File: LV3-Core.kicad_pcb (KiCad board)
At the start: 2 copper layers, 114.3 x 59.1 mm, 81 parts, among them IC1 TLV74033PDBVR, J1 Conn_01x02_Pin, J2 USB_C_Receptacle_USB2.0_16P, J3 Conn_01x01, J4 Conn_01x40_Socket, J5 Conn_01x05_Pin, J6 Conn_01x05_Pin, J7 Conn_01x01, J8 FTSH-105-01-L-DV-K-A, J9 Conn_01x02_Pin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

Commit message: layout almost complete
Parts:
- D1: footprint Package_TO_SOT_SMD:SOT-23_Handsoldering -> Package_TO_SOT_SMD:SOT-23W
- D2, D5: footprint Diode_SMD:D_SOD-323 -> Diode_SMD:D_SOD-323_HandSoldering
- moved C19 71.7 mm to (164.8, 96.8), turned to -135 degrees
- moved D6 36.7 mm to (125.1, 80.0), turned to 180 degrees
- moved R2 33.6 mm to (163.6, 69.6), turned to 90 degrees
- moved R9 33.4 mm to (99.8, 85.6), turned to 90 degrees
- moved R5 33.3 mm to (176.3, 69.6), turned to 90 degrees
- moved C28 32.1 mm to (150.9, 77.2), turned to 0 degrees
- moved C11 31.8 mm to (165.4, 69.6), turned to -90 degrees
- moved C12 31.7 mm to (177.9, 69.6), turned to -90 degrees
- moved R18 30.1 mm to (146.8, 97.3), turned to 0 degrees
- moved D2 29.3 mm to (99.8, 91.7), turned to -90 degrees
- moved D3 29.2 mm to (125.1, 75.6)
- moved IC1 29.0 mm to (149.1, 80.3), turned to -90 degrees
- moved U4 29.0 mm to (100.8, 75.4)
- moved S3 29.0 mm to (182.9, 68.6), turned to 0 degrees
- moved R8 28.9 mm to (98.9, 88.4)
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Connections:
- R6 pad 1: PRIMARY_CAN- -> PRIMARY_CAN+
- R7 pad 1: AUX_CAN- -> AUX_CAN+
- S4 pad 2: PRIMARY_CAN+ -> PRIMARY_CAN-
- S5 pad 2: AUX_CAN+ -> AUX_CAN-
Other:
- board size 114.3 x 59.1 mm -> 114.3 x 57.2 mm
- board text added: "+"
- board text added: "-"
- board text added: "12V"
- board text added: "5V"
- board text added: "AUX CAN"
- board text added: "AUX CAN TERMINATION"
- board text added: "BOOT0 PB8"
- board text added: "CAN+"
- board text added: "CAN-"
- board text added: "GND"
- board text added: "OFF"
- board text added: "ON"
- board text added: "PRIMARY CAN TERMINATION"
- board text added: "RESET"
- board text added: "SWD"
- board text added: "USR1 PC13"

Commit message: completed layout and routing
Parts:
- added D10: LED, LED_SMD:LED_0603_1608Metric_Pad1.05x0.95mm_HandSolder, F.Cu at (106.7, 66.0)
- added D11: LED, LED_SMD:LED_0603_1608Metric_Pad1.05x0.95mm_HandSolder, F.Cu at (116.8, 66.0)
- added D12: LED, LED_SMD:LED_0603_1608Metric_Pad1.05x0.95mm_HandSolder, F.Cu at (127.0, 66.0)
- added D9: LED, LED_SMD:LED_0603_1608Metric_Pad1.05x0.95mm_HandSolder, F.Cu at (169.9, 79.0)
- added R21: 470, Resistor_SMD:R_0603_1608Metric_Pad0.98x0.95mm_HandSolder, F.Cu at (169.9, 80.8)
- added R22: 470, Resistor_SMD:R_0603_1608Metric_Pad0.98x0.95mm_HandSolder, F.Cu at (104.9, 66.0)
- added R23: 470, Resistor_SMD:R_0603_1608Metric_Pad0.98x0.95mm_HandSolder, F.Cu at (115.1, 66.0)
- added R24: 470, Resistor_SMD:R_0603_1608Metric_Pad0.98x0.95mm_HandSolder, F.Cu at (125.2, 66.0)
- moved C19 0.99 mm to (164.1, 96.1)
- moved C27 0.81 mm to (162.9, 95.0)
- moved R7 0.76 mm to (198.9, 89.4)
- moved C8 0.67 mm to (164.7, 86.1), turned to 45 degrees
- moved C9 0.66 mm to (165.9, 87.2), turned to 45 degrees
- moved L1 0.62 mm to (164.7, 83.7)
- moved C7 0.58 mm to (167.3, 83.6)
- moved R4 0.38 mm to (137.5, 73.7)
- moved R3 0.36 mm to (142.2, 73.7)
- moved C23 0.15 mm to (124.0, 71.5)
- moved S5 0.10 mm to (192.8, 94.8)
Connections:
- J4 pad 10: unconnected-(J4-Pin_10-Pad10) -> IO_PC7
- J4 pad 11: unconnected-(J4-Pin_11-Pad11) -> IO_PC8
- J4 pad 12: unconnected-(J4-Pin_12-Pad12) -> IO_PC9
- J4 pad 13: unconnected-(J4-Pin_13-Pad13) -> FDCAN3_RX
- J4 pad 14: unconnected-(J4-Pin_14-Pad14) -> IO_PA9
- J4 pad 15: unconnected-(J4-Pin_15-Pad15) -> IO_PA10
- J4 pad 16: unconnected-(J4-Pin_16-Pad16) -> IO_PB10
- J4 pad 17: unconnected-(J4-Pin_17-Pad17) -> IO_PB2
- J4 pad 18: unconnected-(J4-Pin_18-Pad18) -> IO_PB1
- J4 pad 19: unconnected-(J4-Pin_19-Pad19) -> IO_PC5
- J4 pad 20: unconnected-(J4-Pin_20-Pad20) -> IO_PC4
- J4 pad 21: unconnected-(J4-Pin_21-Pad21) -> IO_PA7
- J4 pad 22: unconnected-(J4-Pin_22-Pad22) -> IO_PA5
- J4 pad 23: unconnected-(J4-Pin_23-Pad23) -> IO_PA3
- J4 pad 24: unconnected-(J4-Pin_24-Pad24) -> IO_PC3
- J4 pad 25: unconnected-(J4-Pin_25-Pad25) -> IO_PC2
- J4 pad 26: unconnected-(J4-Pin_26-Pad26) -> IO_PC1
- J4 pad 27: unconnected-(J4-Pin_27-Pad27) -> IO_PC0
- J4 pad 28: unconnected-(J4-Pin_28-Pad28) -> IO_PC15
- J4 pad 29: unconnected-(J4-Pin_29-Pad29) -> IO_PC14
- J4 pad 30: unconnected-(J4-Pin_30-Pad30) -> IO_PA15
- J4 pad 31: unconnected-(J4-Pin_31-Pad31) -> IO_PC10
- J4 pad 32: unconnected-(J4-Pin_32-Pad32) -> IO_PC11
- J4 pad 33: unconnected-(J4-Pin_33-Pad33) -> IO_PC12
- J4 pad 34: unconnected-(J4-Pin_34-Pad34) -> IO_PD2
- J4 pad 35: unconnected-(J4-Pin_35-Pad35) -> FDCAN3_TX
- J4 pad 36: unconnected-(J4-Pin_36-Pad36) -> IO_PB6
- J4 pad 37: unconnected-(J4-Pin_37-Pad37) -> IO_PB7
- J4 pad 38: unconnected-(J4-Pin_38-Pad38) -> IO_PB9
- J4 pad 39: unconnected-(J4-Pin_39-Pad39) -> GND
- J4 pad 40: unconnected-(J4-Pin_40-Pad40) -> GND
- J4 pad 7: unconnected-(J4-Pin_7-Pad7) -> IO_PB11
- J4 pad 8: unconnected-(J4-Pin_8-Pad8) -> IO_PB15
- J4 pad 9: unconnected-(J4-Pin_9-Pad9) -> IO_PC6
- U1 pad 19: LED_USR -> IO_PA5
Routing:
- net GND: track 6.07 -> 644.3 mm, vias 0 -> 27
- net +3.3V: track 9.74 -> 210.3 mm, vias 0 -> 2
- net +5V: track 0.00 -> 185.1 mm, vias 0 -> 4
- net V_SENSE_12: track 0.00 -> 83.9 mm, vias 0 -> 2
- net FDCAN3_RX: track 0.00 -> 82.2 mm, vias 0 -> 4
- net USB+: track 0.00 -> 64.2 mm, vias 0 -> 2
- net USB-: track 0.00 -> 62.5 mm, vias 0 -> 2
- net IO_PB11: track 0.00 -> 57.8 mm
- net +12V: track 0.00 -> 57.4 mm, vias 0 -> 2
- net IO_PB15: track 0.00 -> 53.6 mm
- net IO_PC6: track 0.00 -> 51.2 mm
- net FDCAN3_TX: track 0.00 -> 49.1 mm, vias 0 -> 2
- net IO_PC7: track 0.00 -> 48.9 mm
- net NRST: track 0.00 -> 48.7 mm, vias 0 -> 2
- net IO_PC8: track 0.00 -> 46.6 mm
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- added copper zone on F.Cu, net +5V_BUCK
- added copper zone on B.Cu, net GND
- added copper zone on F.Cu, net GND
- added copper zone on F.Cu, net Net-(D3-K)
- added copper zone on B.Cu, net Net-(U4-EN)
- added copper zone on F.Cu, net Net-(U4-EN)
- added copper zone on F.Cu, net Net-(U4-SW)
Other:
- board text added: "12V IN"
- board text added: "3.3V"
- board text added: "5V IN"
- board text added: "USR PC13"
- board text added: "USR/PA5"
- board text removed: "USR1 PC13"

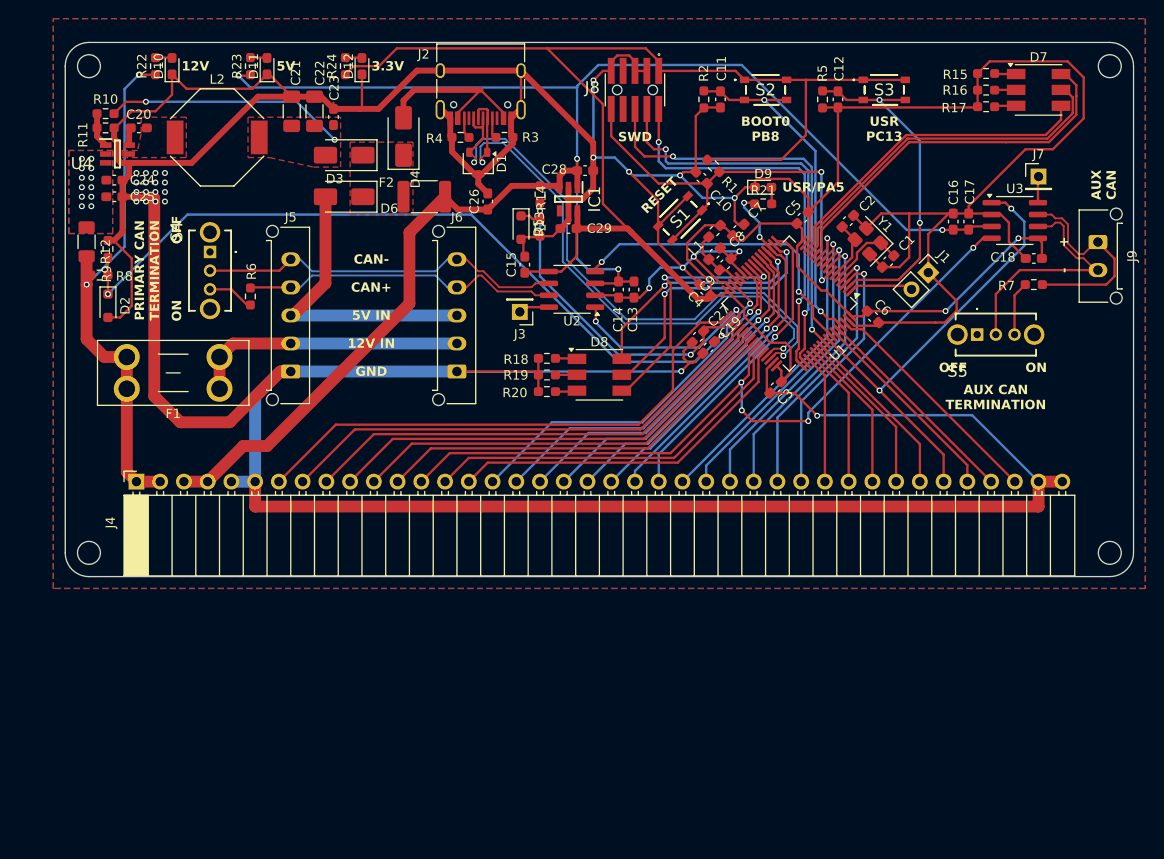
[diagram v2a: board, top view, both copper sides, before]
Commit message: adjusted input power section, completed silkscreen text
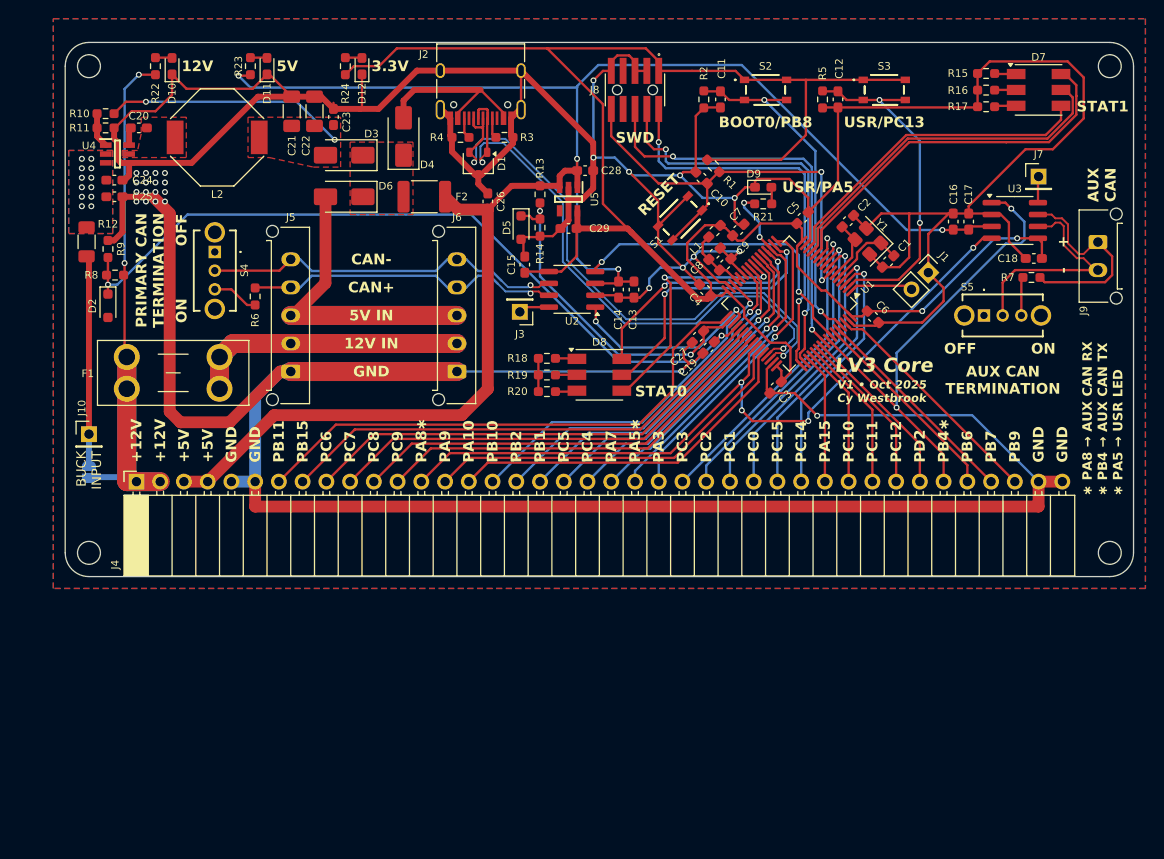
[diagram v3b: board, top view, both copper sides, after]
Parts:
- added J10: Conn_01x01, Connector_PinHeader_2.54mm:PinHeader_1x01_P2.54mm_Vertical, F.Cu at (97.8, 105.4)
- added JP1: SolderJumper_2_Open, Jumper:SolderJumper-2_P1.3mm_Open_RoundedPad1.0x1.5mm, B.Cu at (97.8, 109.5)
- moved S5 2.17 mm to (193.5, 92.7)
- moved R8 1.67 mm to (100.6, 88.4), turned to 180 degrees
- moved R7 0.80 mm to (198.6, 88.6)
- moved R6 0.51 mm to (115.6, 90.7)
- moved S4 0.51 mm to (111.3, 85.9)
- renumbered IC1 to U5
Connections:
- R12 pad 1: +12V -> Net-(J10-Pin_1)
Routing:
- net +12V_IN: track 29.4 -> 58.8 mm
- net Net-(J10-Pin_1): track 0.00 -> 22.4 mm
- net +5V_BUS: track 32.2 -> 50.0 mm
- net +12V: track 57.4 -> 72.4 mm
- net +5V: track 185.1 -> 195.9 mm
- net GND: track 644.3 -> 637.9 mm
- net Net-(S5-NO): track 6.19 -> 4.13 mm
- net AUX_CAN-: track 26.2 -> 24.1 mm
- net FDCAN3_TX: track 49.1 -> 51.1 mm
- net Net-(S4-NO): track 5.01 -> 4.50 mm
- net PRIMARY_CAN+: track 34.4 -> 34.0 mm, vias 0 -> 1
- net PRIMARY_CAN-: track 39.2 -> 38.9 mm, vias 0 -> 1
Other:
- board text added: "+12V"
- board text added: "+5V"
- board text added: "12V TO BUCK"
- board text added: "BOOT0/PB8"
- board text added: "BUCK INPUT"
- board text added: "LV3 Core"
- board text added: "PA10"
- board text added: "PA15"
- board text added: "PA3"
- board text added: "PA5∗"
- board text added: "PA7"
- board text added: "PA8∗"
- board text added: "PA9"
- board text added: "PB1"
- board text added: "PB10"
- board text added: "PB11"
- board text added: "PB15"
- board text added: "PB2"
- board text added: "PB4∗"
- board text added: "PB6"
- board text added: "PB7"
- board text added: "PB9"
- board text added: "PC0"
- board text added: "PC1"
- board text added: "PC10"
- board text added: "PC11"
- board text added: "PC12"
- board text added: "PC14"
- board text added: "PC15"
- board text added: "PC2"
- board text added: "PC3"
- board text added: "PC4"
- board text added: "PC5"
- board text added: "PC6"
- board text added: "PC7"
- board text added: "PC8"
- board text added: "PC9"
- board text added: "PD2"
- board text added: "STAT0"
- board text added: "STAT1"
- board text added: "USR/PC13"
- board text added: "V1 • Oct 2025 Cy Westbrook"
- board text added: "∗ PA8 → AUX CAN RX ∗ PB4 → AUX CAN TX ∗ PA5 → USR LED"
- board text removed: "BOOT0 PB8"
- board text removed: "USR PC13"

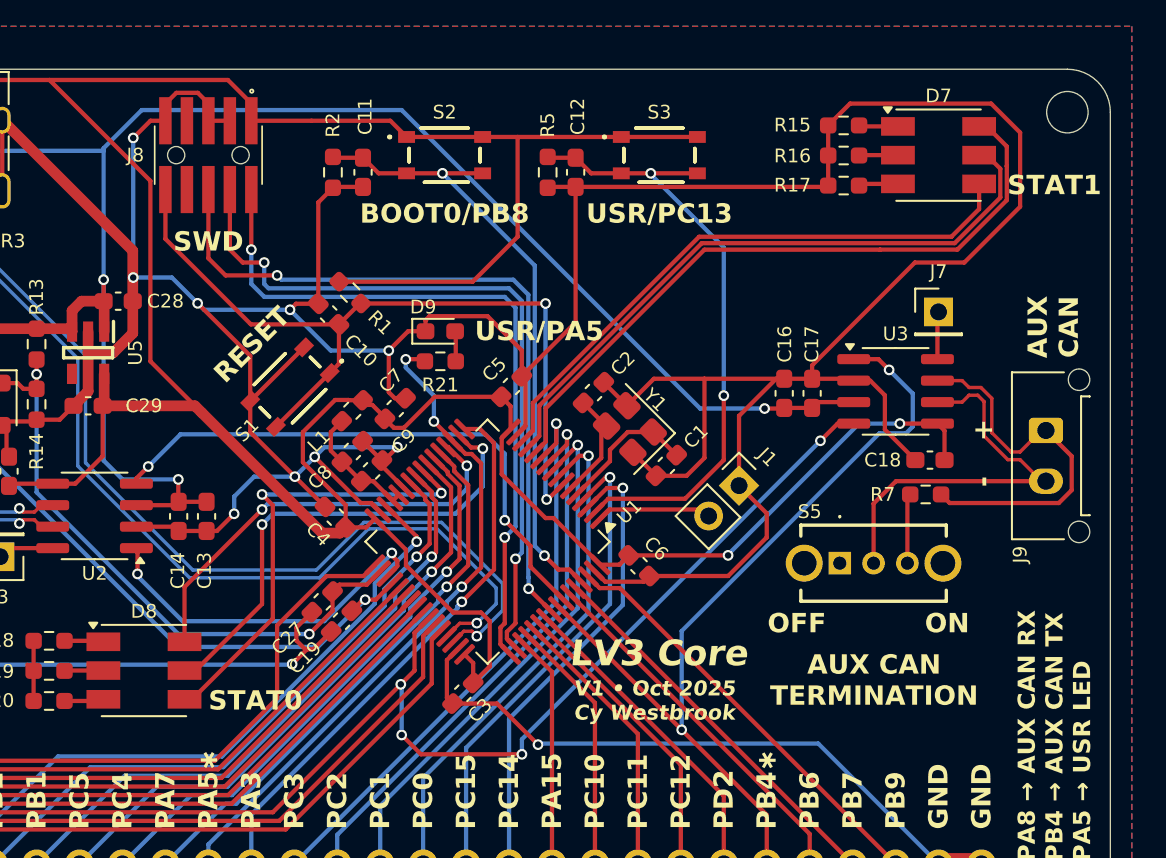
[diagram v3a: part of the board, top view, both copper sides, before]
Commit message: move aux can termination switch to make room for silkscreen
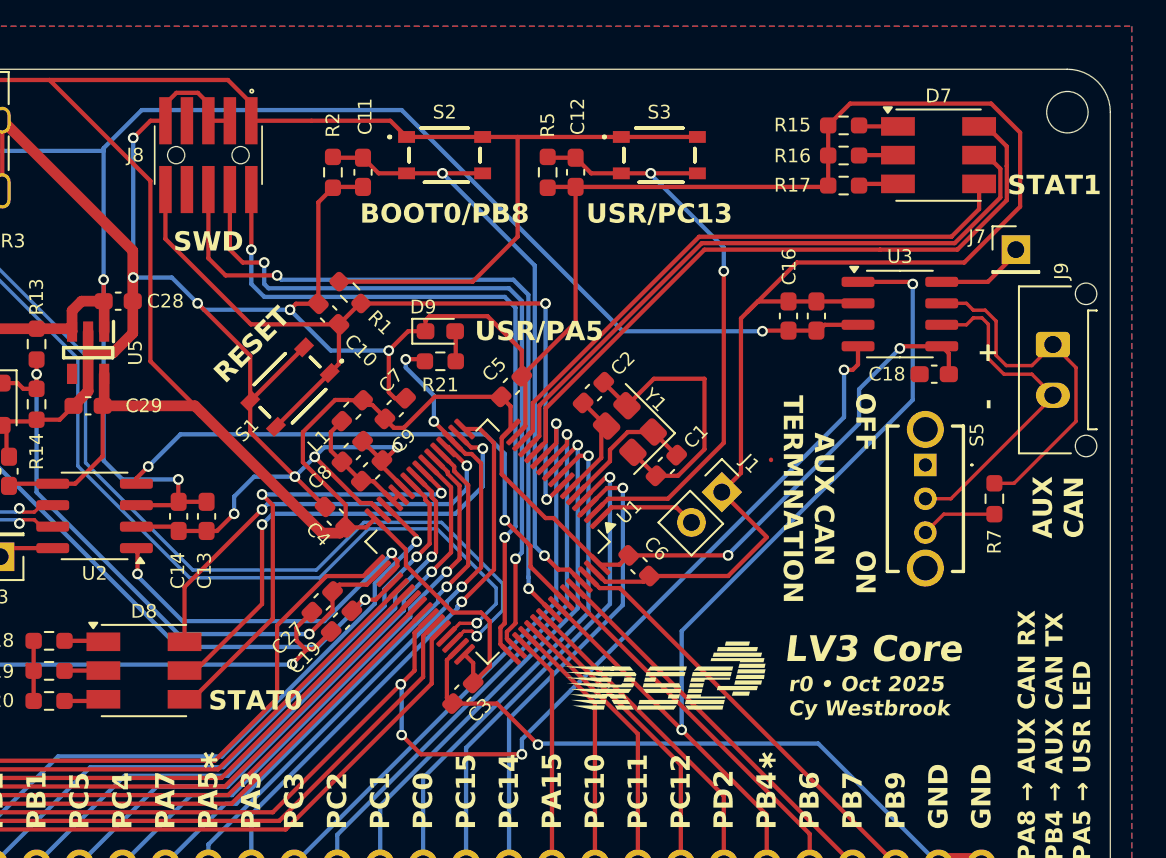
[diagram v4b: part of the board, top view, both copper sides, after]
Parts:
- moved S5 7.71 mm to (198.6, 86.9), turned to -90 degrees
- moved J7 5.87 mm to (204.0, 74.2)
- moved J9 5.10 mm to (206.2, 79.8)
- moved C18 5.09 mm to (199.1, 81.5)
- moved U3 4.58 mm to (197.1, 78.0)
- moved C16 4.58 mm to (190.5, 78.1)
- moved C17 4.58 mm to (192.2, 78.1)
- moved R7 4.07 mm to (202.7, 88.9), turned to -90 degrees
- moved J1 1.09 mm to (186.6, 88.5)
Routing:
- net FDCAN3_TX: track 51.1 -> 55.6 mm
- net FDCAN3_RX: track 82.2 -> 86.6 mm
- net AUX_CAN-: track 24.1 -> 20.2 mm
- net GND: track 637.9 -> 634.1 mm
- net +3.3V: track 210.2 -> 212.9 mm
- net Net-(J7-Pin_1): track 2.82 -> 5.07 mm
- net +5V: track 195.9 -> 194.3 mm
- net AUX_CAN+: track 22.3 -> 21.3 mm
- net Net-(J1-Pin_2): track 6.80 -> 6.04 mm
- net BTN_USR1: track 37.0 -> 36.4 mm
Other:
- board text added: "r0 • Oct 2025 Cy Westbrook"
- board text removed: "V1 • Oct 2025 Cy Westbrook"

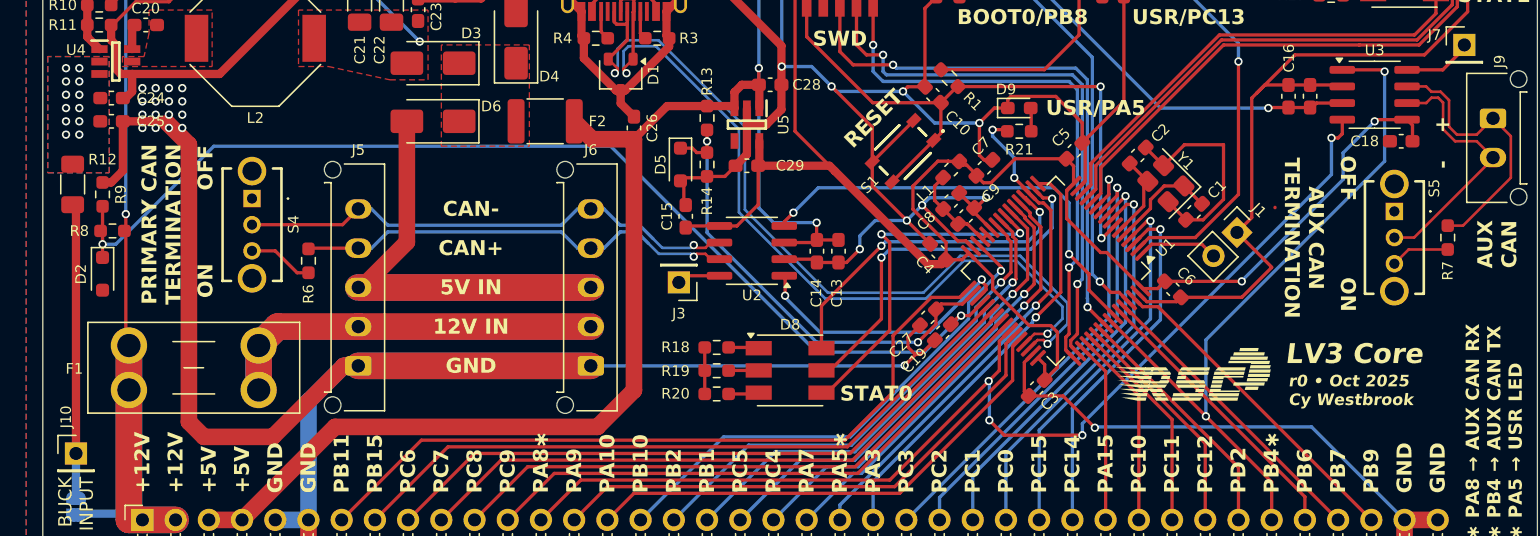
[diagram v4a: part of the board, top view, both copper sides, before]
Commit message: minor silkscreen changes, add reverse block diode for 12v ORDER 23 october 2025
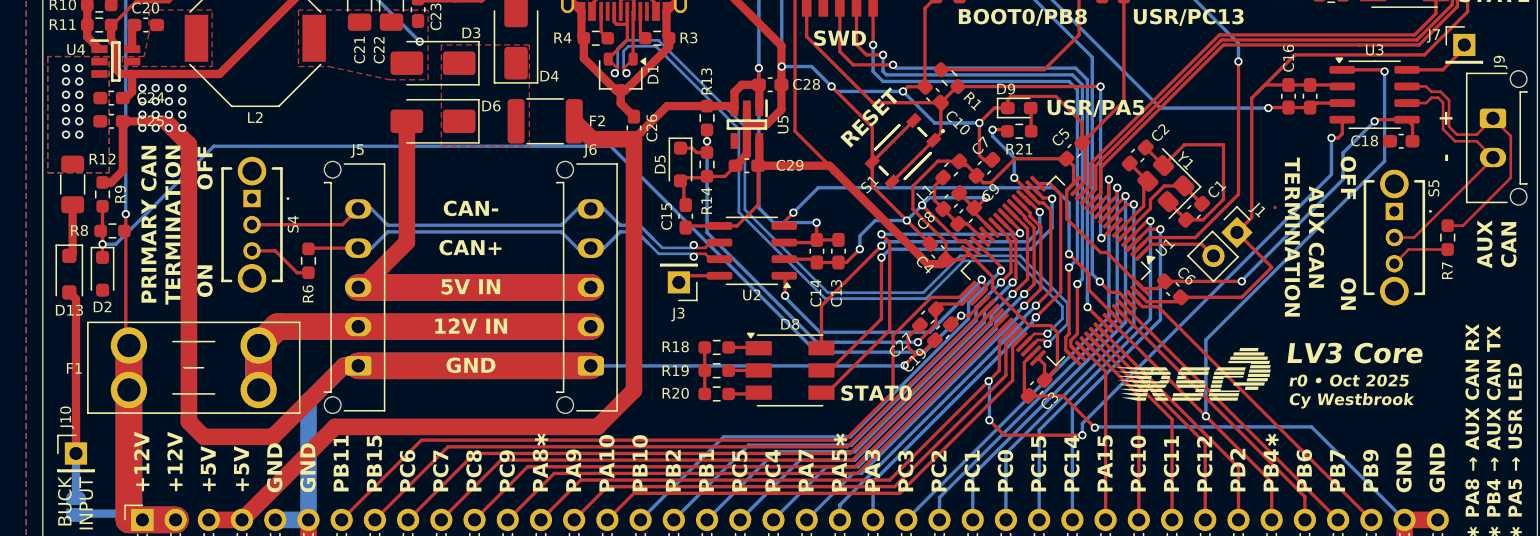
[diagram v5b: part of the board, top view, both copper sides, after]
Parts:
- added D13: D_Schottky, Diode_SMD:D_SOD-123F, F.Cu at (97.3, 91.7)
- R15, R18: value 100 -> 120
- R22: value 470 -> 2.2k
- R24: value 470 -> 120
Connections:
- J10 pad 1: Net-(J10-Pin_1) -> Net-(D13-A)
- JP1 pad 2: Net-(J10-Pin_1) -> Net-(D13-A)
- R12 pad 1: Net-(J10-Pin_1) -> Net-(D13-K)
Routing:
- net Net-(J10-Pin_1): track 22.4 -> 0.00 mm
- net Net-(D13-A): track 0.00 -> 15.8 mm
- net Net-(D13-K): track 0.00 -> 4.01 mm
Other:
- board text added: "JLCJLCJLCJLC"
- board text added: "Rutgers Solar Car"
